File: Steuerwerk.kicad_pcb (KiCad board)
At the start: 2 copper layers, 100 x 160 mm, 124 parts, among them J1 2PinTerminalBlocktg, J10 2PinTerminalBlocktg, J11 2PinTerminalBlocktg, J12 2PinTerminalBlocktg, J2 2PinTerminalBlocktg, J3 3PinTerminalBlocktg, J4 3PinTerminalBlocktg, J5 2PinTerminalBlocktg, J6 2PinTerminalBlocktg, J7 2PinTerminalBlocktg, J8 2PinTerminalBlocktg, J9 2PinTerminalBlocktg, Q1 Q_PNP_BCE, U1 74ls240, U2 74541, U3 74LS161, U4 74LS138, U5 74LS138, U6 74541, U7 74LS374, U8 74LS374

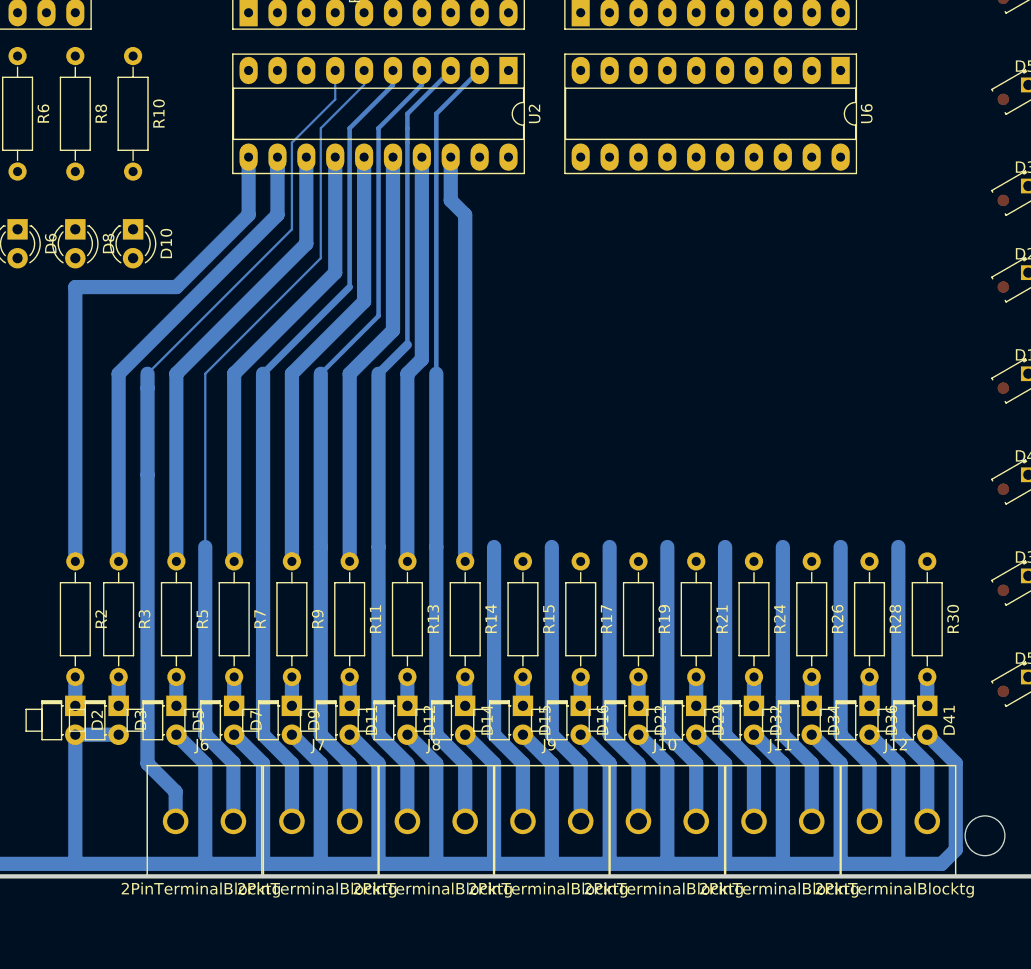
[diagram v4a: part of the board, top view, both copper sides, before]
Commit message: Leiterbahnen Korrigiert
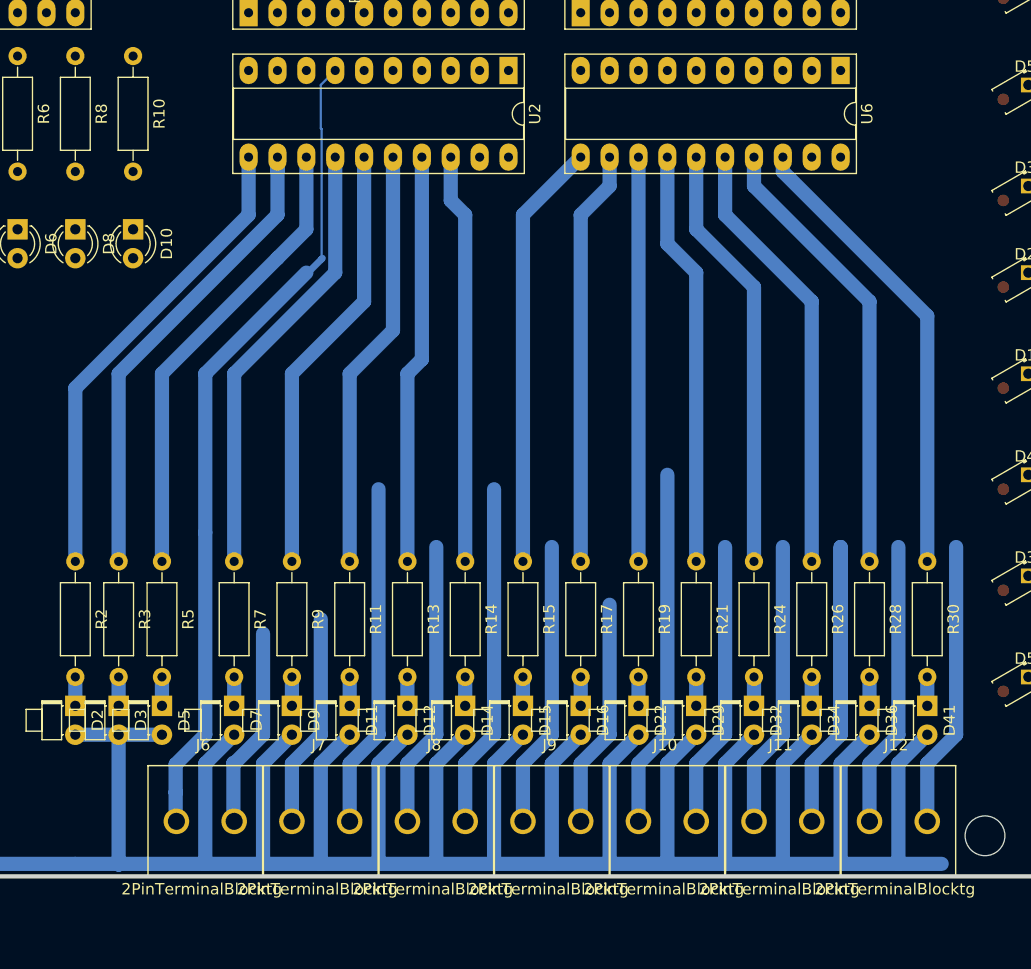
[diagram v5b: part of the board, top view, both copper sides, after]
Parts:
- moved D5 1.27 mm to (63.5, 189.2)
- moved R5 1.27 mm to (63.5, 176.5)
- moved J6 0.07 mm to (67.3, 199.4)
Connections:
- J10 pad 1: Net-(J10-Pad1) -> /11
- J10 pad 2: /11 -> Net-(J10-Pad2)
- J11 pad 1: Net-(J11-Pad1) -> /13
- J11 pad 2: /13 -> Net-(J11-Pad2)
- J12 pad 1: /16 -> /15
- J12 pad 2: /15 -> /16
- J9 pad 1: Net-(J9-Pad1) -> /9
- J9 pad 2: /9 -> Net-(J9-Pad2)
- U6 pad 4: Net-(J11-Pad1) -> Net-(J11-Pad2)
- U6 pad 6: Net-(J10-Pad1) -> Net-(J10-Pad2)
- U6 pad 8: Net-(J9-Pad1) -> Net-(J9-Pad2)
- U8 pad 15: Net-(J11-Pad1) -> Net-(J11-Pad2)
- U8 pad 5: Net-(J9-Pad1) -> Net-(J9-Pad2)
- U8 pad 9: Net-(J10-Pad1) -> Net-(J10-Pad2)
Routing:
- net Net-(J6-Pad2): track 72.9 -> 17.7 mm
- net /5: track 71.8 -> 18.8 mm
- net /7: track 69.7 -> 25.2 mm
- net Net-(J11-Pad2): track 0.00 -> 41.7 mm
- net Net-(R30-Pad1): track 0.00 -> 40.8 mm
- net Net-(J7-Pad2): track 70.8 -> 30.3 mm
- net Net-(R28-Pad1): track 0.00 -> 39.8 mm
- net Net-(R26-Pad1): track 0.00 -> 38.7 mm
- net /enAkku: track 68.7 -> 30.3 mm
- net Net-(R24-Pad1): track 0.00 -> 37.7 mm
- net Net-(R15-Pad1): track 0.00 -> 37.7 mm
- net Net-(R21-Pad1): track 0.00 -> 36.6 mm
- net Net-(R17-Pad1): track 0.00 -> 36.6 mm
- net Net-(R19-Pad1): track 0.00 -> 35.6 mm
- net Net-(J9-Pad1): track 25.2 -> 0.00 mm
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
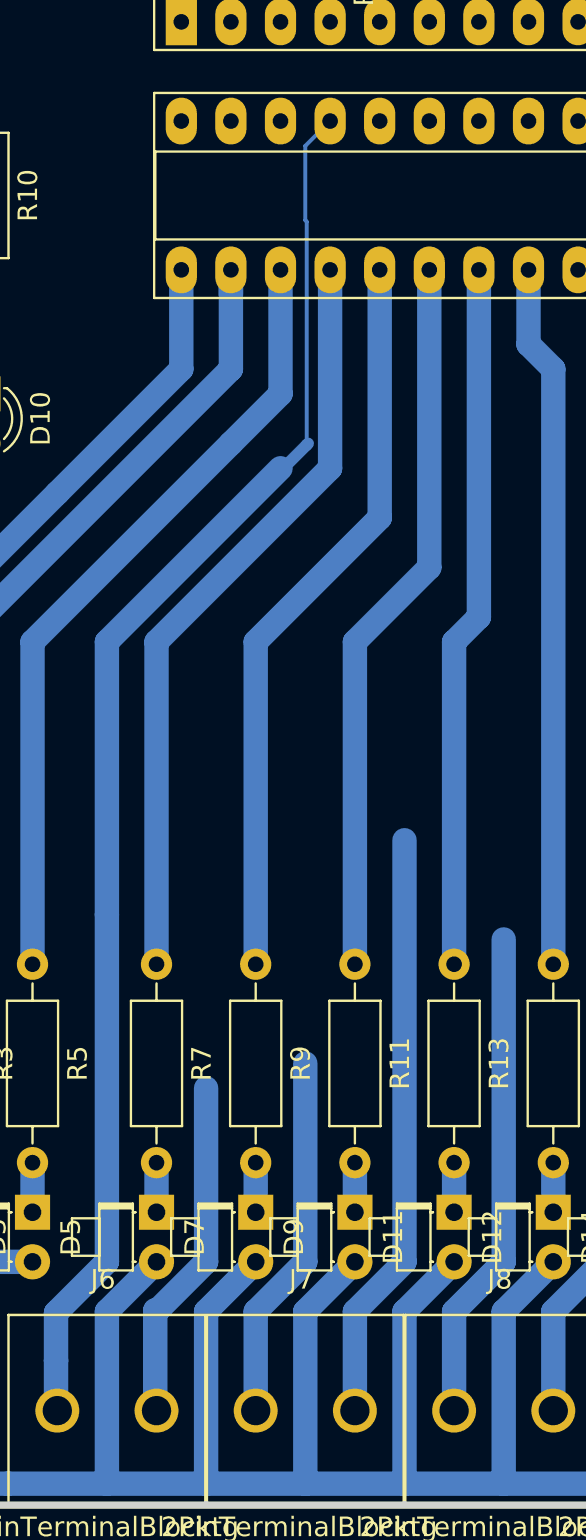
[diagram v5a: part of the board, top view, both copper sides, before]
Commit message: Library Datei zur ToDo Liste hinzugefügt
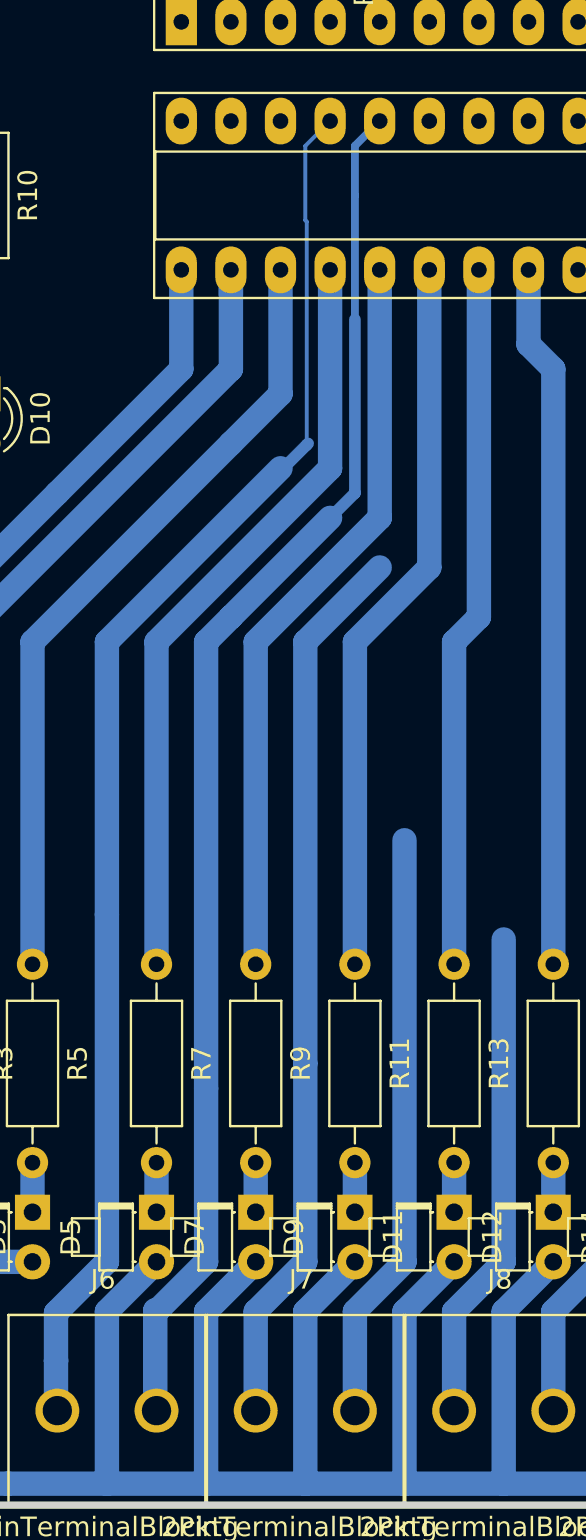
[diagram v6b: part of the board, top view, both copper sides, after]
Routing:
- net Net-(J6-Pad2): track 17.7 -> 70.9 mm
- net /5: track 18.8 -> 45.8 mm
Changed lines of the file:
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@@
     (thickness 1.6)
     (drawings 0)
-    (tracks 177)
+    (tracks 187)
     (zones 0)
     (modules 124)
@@
   )
   (setup
-    (last_trace_width 0.2)
+    (last_trace_width 0.4)
     (user_trace_width 0.2)
     (user_trace_width 0.4)
@@
   (segment (start 76.344998 151.13) (end 77.542499 149.932499) (width 0.6) (layer B.Cu) (net 111))
   (segment (start 77.542499 149.932499) (end 77.614998 149.86) (width 0.6) (layer B.Cu) (net 111))
+  (segment (start 81.28 156.21) (end 77.47 160.02) (width 1.25) (layer B.Cu) (net 112))
   (segment (start 74.93 194.31) (end 77.47 191.77) (width 1.25) (layer B.Cu) (net 112))
-  (segment (start 74.93 199.39) (end 74.93 194.31) (width 1.25) (layer B.Cu) (net 112) (status 400000))
+  (segment (start 74.93 194.31) (end 74.93 199.39) (width 1.25) (layer B.Cu) (net 112) (status 800000))
   (segment (start 77.47 191.77) (end 77.47 181.61) (width 1.25) (layer B.Cu) (net 112))
+  (segment (start 77.47 160.02) (end 77.47 181.61) (width 1.25) (layer B.Cu) (net 112))
   (segment (start 85.09 194.31) (end 87.63 191.77) (width 1.25) (layer B.Cu) (net 113))
   (segment (start 85.09 199.39) (end 85.09 194.31) (width 1.25) (layer B.Cu) (net 113) (status 400010))
@@
   (segment (start 115.57 199.39) (end 115.57 194.31) (width 1.25) (layer B.Cu) (net 115) (status 400010))
   (segment (start 118.11 191.77) (end 118.11 175.26) (width 1.25) (layer B.Cu) (net 115))
+  (segment (start 80.01 137.16) (end 80.01 134.62) (width 0.4) (layer B.Cu) (net 120))
+  (segment (start 80.01 152.4) (end 78.74 153.67) (width 0.6) (layer B.Cu) (net 120))
+  (segment (start 72.39 182.88) (end 72.39 160.02) (width 1.25) (layer B.Cu) (net 120))
+  (segment (start 69.85 194.31) (end 72.39 191.77) (width 1.25) (layer B.Cu) (net 120))
+  (segment (start 72.39 191.77) (end 72.39 182.88) (width 1.25) (layer B.Cu) (net 120))
+  (segment (start 69.784282 194.31) (end 69.85 194.31) (width 1.25) (layer B.Cu) (net 120))
+  (segment (start 72.39 160.02) (end 73.66 158.75) (width 1.25) (layer B.Cu) (net 120))
+  (segment (start 78.74 153.67) (end 73.66 158.75) (width 1.25) (layer B.Cu) (net 120))
+  (segment (start 80.01 143.51) (end 80.01 152.4) (width 0.6) (layer B.Cu) (net 120))
+  (segment (start 80.01 137.16) (end 80.01 143.51) (width 0.4) (layer B.Cu) (net 120))
+  (segment (start 80.01 134.62) (end 81.28 133.35) (width 0.4) (layer B.Cu) (net 120) (status 800000))
   (segment (start 123.19 191.77) (end 123.19 175.26) (width 1.25) (layer B.Cu) (net 124))
   (segment (start 123.19 191.77) (end 123.19 175.26) (width 1.25) (layer B.Cu) (net 124))
@@
   (segment (start 64.704282 199.39) (end 64.704282 196.85) (width 1.25) (layer B.Cu) (net 111) (status 400000))
   (segment (start 64.704282 196.85) (end 64.704282 196.784282) (width 1.25) (layer B.Cu) (net 111))
-  (segment (start 69.784282 194.31) (end 69.85 194.31) (width 1.25) (layer B.Cu) (net 120))
-  (segment (start 72.39 191.77) (end 72.39 182.88) (width 1.25) (layer B.Cu) (net 120))
-  (segment (start 69.85 194.31) (end 72.39 191.77) (width 1.25) (layer B.Cu) (net 120))
   (segment (start 69.784282 199.39) (end 69.784282 194.31) (width 1.25) (layer B.Cu) (net 120) (status 400000))
   (segment (start 69.784282 194.31) (end 69.784282 194.244282) (width 1.25) (layer B.Cu) (net 120))

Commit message: Weitere Leiterbahnen hinzugefügt und den überflüssigen IC entfernt
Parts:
- removed the U8 at (71.1, 128.3)
- removed the U8 at (100.3, 128.3)
- added U8: 74LS374, Housings_DIP:DIP-20_W7.62mm_Socket_LongPads, F.Cu at (100.2, 127.8)
- moved U7 154.2 mm to (71.2, 127.8), turned to 90 degrees
- moved D43 78.1 mm to (104.1, 69.9)
- moved D17 75.6 mm to (201.0, 115.8)
- moved D37 75.6 mm to (201.0, 133.6)
- moved D21 75.6 mm to (201.0, 106.9)
- moved D39 75.6 mm to (201.0, 99.3)
- moved D40 75.6 mm to (201.0, 72.6)
- moved D46 75.6 mm to (201.0, 124.7)
- moved D51 75.6 mm to (201.0, 81.5)
- moved D56 75.6 mm to (201.0, 90.4)
- moved D59 75.6 mm to (201.0, 142.5)
- moved D20 75.6 mm to (213.7, 133.6)
- moved D23 75.6 mm to (213.7, 115.8)
- moved D26 75.6 mm to (207.4, 133.6)
- moved D35 75.6 mm to (207.4, 115.8)
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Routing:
- net VCC: track 270.5 -> 629.4 mm
- net Net-(D43-Pad1): track 0.00 -> 68.8 mm
- net Net-(D17-Pad1): track 0.00 -> 63.9 mm
- net Net-(D33-Pad1): track 0.00 -> 63.8 mm
- net Net-(D23-Pad1): track 0.00 -> 63.1 mm
- net Net-(R39-Pad2): track 0.00 -> 54.3 mm
- net Net-(D17-Pad2): track 0.00 -> 54.2 mm
- net Net-(D23-Pad2): track 0.00 -> 54.1 mm
- net Net-(D21-Pad2): track 0.00 -> 54.0 mm
- net Net-(D30-Pad2): track 0.00 -> 53.8 mm
- net Net-(D46-Pad2): track 0.00 -> 53.4 mm
- net Net-(R27-Pad2): track 0.00 -> 53.3 mm
- net Net-(R38-Pad2): track 0.00 -> 53.2 mm
- net Net-(D47-Pad2): track 0.00 -> 52.5 mm
- net Net-(D43-Pad2): track 0.00 -> 52.4 mm
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
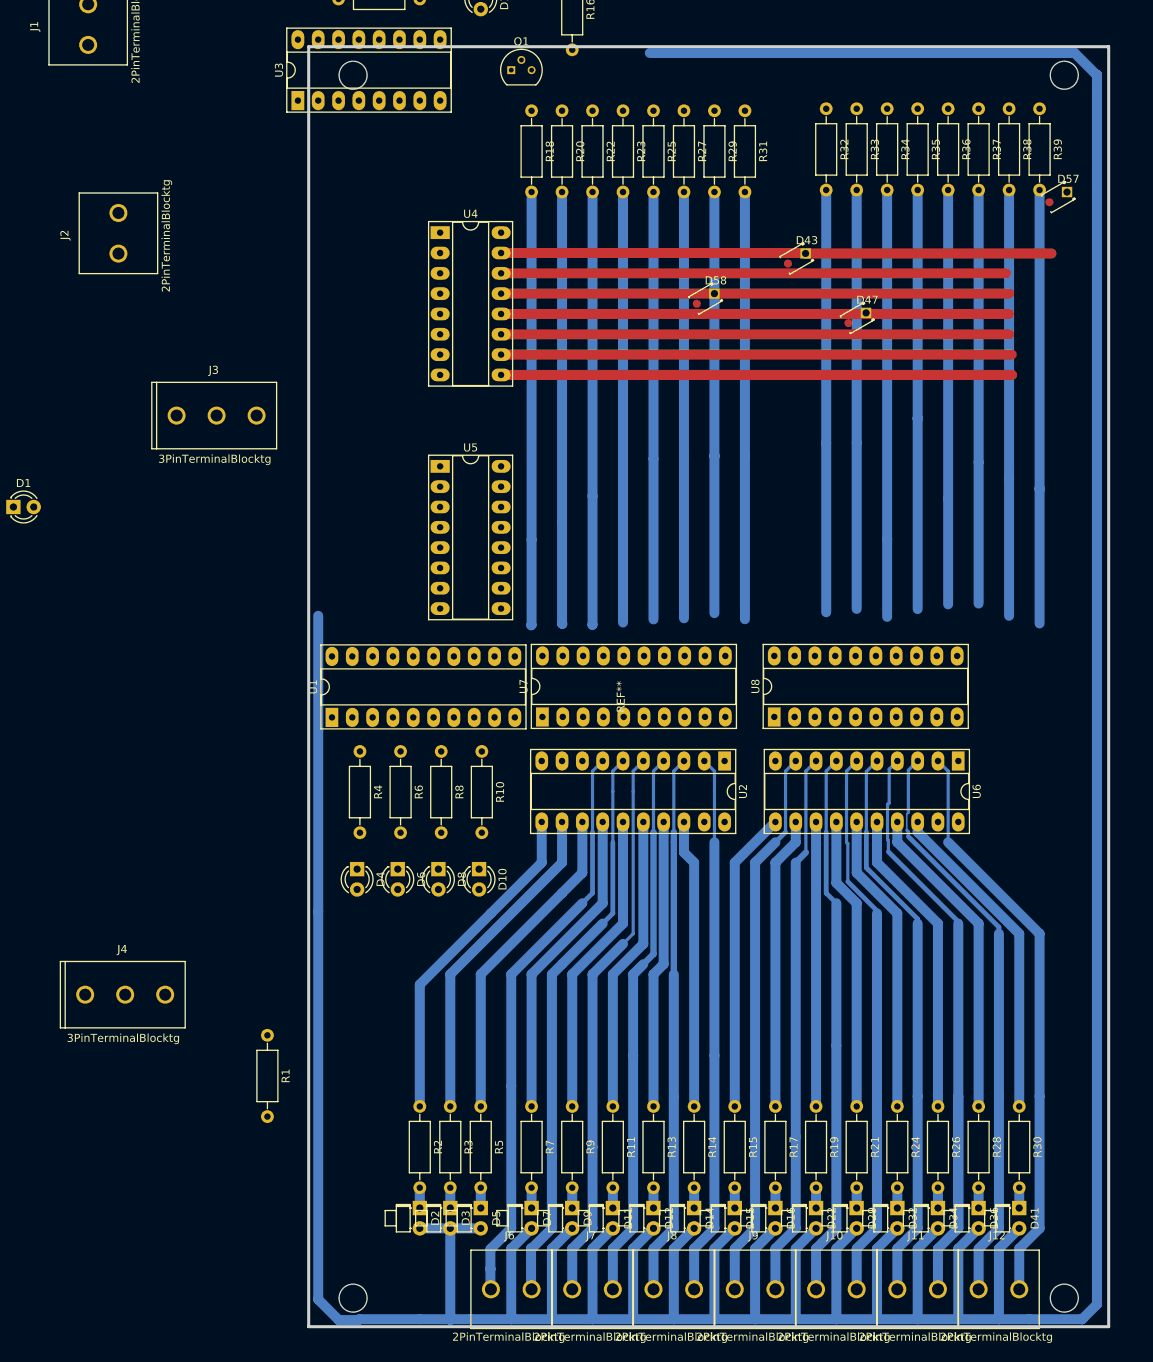
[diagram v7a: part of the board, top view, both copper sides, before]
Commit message: Teile verschoben um mehr Platz zu kriegen
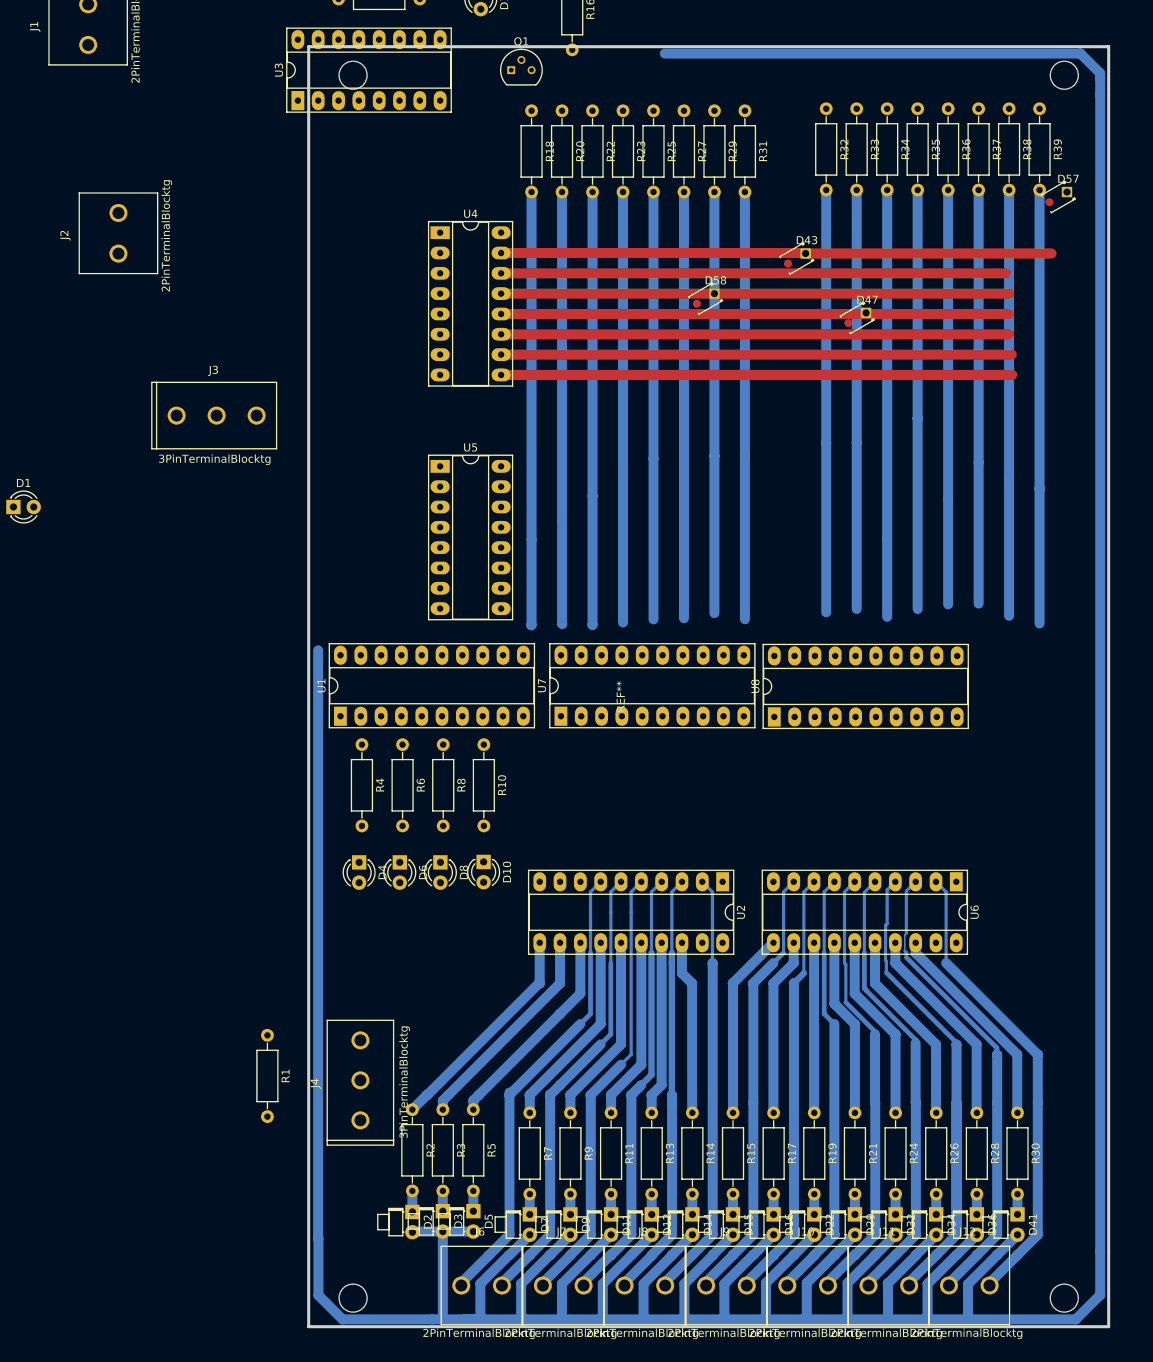
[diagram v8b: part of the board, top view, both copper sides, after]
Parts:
- moved J4 31.3 mm to (48.5, 173.3), turned to 90 degrees
- moved U2 15.1 mm to (93.7, 148.4)
- moved U6 15.1 mm to (122.9, 148.4)
- moved J12 3.74 mm to (124.6, 198.9)
- moved J6 3.73 mm to (63.6, 198.9)
- moved J7 3.69 mm to (73.8, 198.9)
- moved J8 3.65 mm to (84.0, 198.9)
- moved J11 3.64 mm to (114.5, 198.9)
- moved J10 3.63 mm to (104.4, 198.9)
- moved J9 3.62 mm to (94.2, 198.9)
- moved U7 2.31 mm to (73.5, 127.7)
- moved U1 1.07 mm to (46.0, 127.7)
- moved D10 1.07 mm to (63.9, 146.0)
- moved D2 1.04 mm to (55.0, 189.7)
- moved D3 1.01 mm to (58.8, 189.6)
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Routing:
- net Net-(R5-Pad1): track 40.8 -> 26.4 mm
- net Net-(R3-Pad1): track 42.6 -> 28.2 mm
- net Net-(J10-Pad2): track 69.2 -> 54.8 mm
- net /11: track 68.1 -> 53.8 mm
- net Net-(J9-Pad2): track 68.1 -> 53.8 mm
- net Net-(J6-Pad2): track 70.9 -> 56.5 mm
- net Net-(R2-Pad1): track 41.9 -> 27.5 mm
- net /7: track 67.6 -> 53.3 mm
- net /15: track 72.4 -> 58.1 mm
- net Net-(J11-Pad2): track 87.8 -> 73.5 mm
- net Net-(R26-Pad1): track 38.7 -> 24.4 mm
- net Net-(R28-Pad1): track 39.8 -> 25.5 mm
- net Net-(R24-Pad1): track 37.7 -> 23.4 mm
- net Net-(R21-Pad1): track 36.6 -> 22.3 mm
- net Net-(R30-Pad1): track 40.8 -> 26.5 mm
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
